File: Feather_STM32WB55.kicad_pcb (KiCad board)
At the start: 4 copper layers, 52.5 x 22.9 mm, 50 parts, among them J1 JST-SH Qwiic, J2 Conn_Battery, J4 Conn_Right, J5 USB_C_Receptacle_USB2.0, J6 Conn_Left, Q1 NTR4171PT1G, SW1 SMD-BUTTON-TOP-DHT-4235A_4P-4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, U1 MCP73831-2-OT, U2 AP2112K-3.3, U3 STM32WB55CGU6, U4 USBLC6-2SC6, Y1 32Mhz

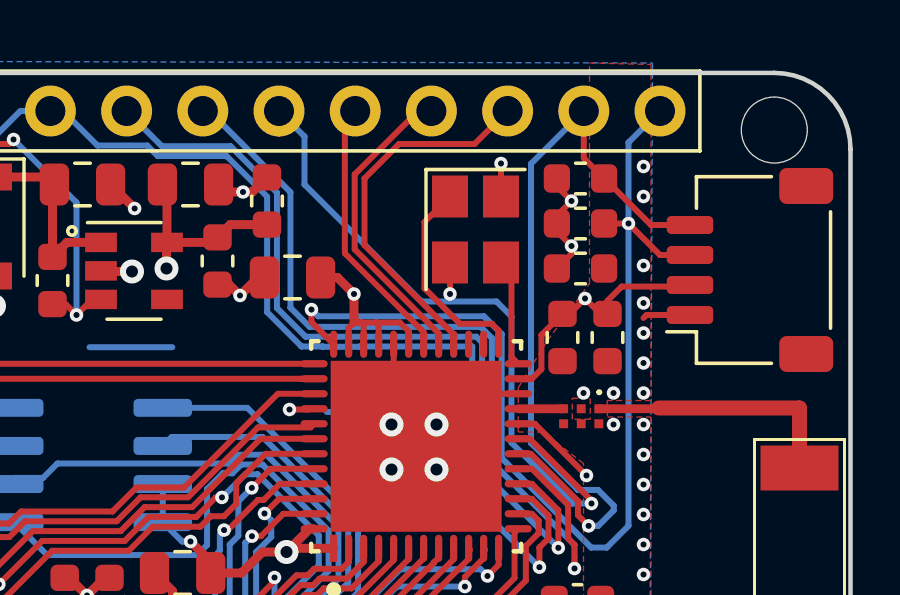
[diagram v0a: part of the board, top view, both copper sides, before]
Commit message: fix: repair STM32WB55 short and restore project libraries (#1)
* docs: improve project discovery and reuse guidance

Describe the historical design and available artifacts from repository evidence. Keep hardware and fabrication outputs unchanged, preserve third-party rights, and make unresolved setup and validation limits visible.

* docs: record completed discoverability delivery

* fix: clear the D10 ground short and restore legacy libraries

Move the overlapping ground via using a controlled before/after zone-refilled DRC comparison. Recover original dependencies and align component identifiers without redesigning the land pattern or guessing the physical stackup. Keep historical fabrication outputs explicitly separate from corrected source.

* docs: record completed source audit delivery

* docs: qualify nightly netlist validation by library resolution

Independent export checks show nightly legacy global-library resolution omits the USB shield pin despite identical cached and global pin geometry. Document the exact cache-only invocation and retain the source without speculative wiring changes.
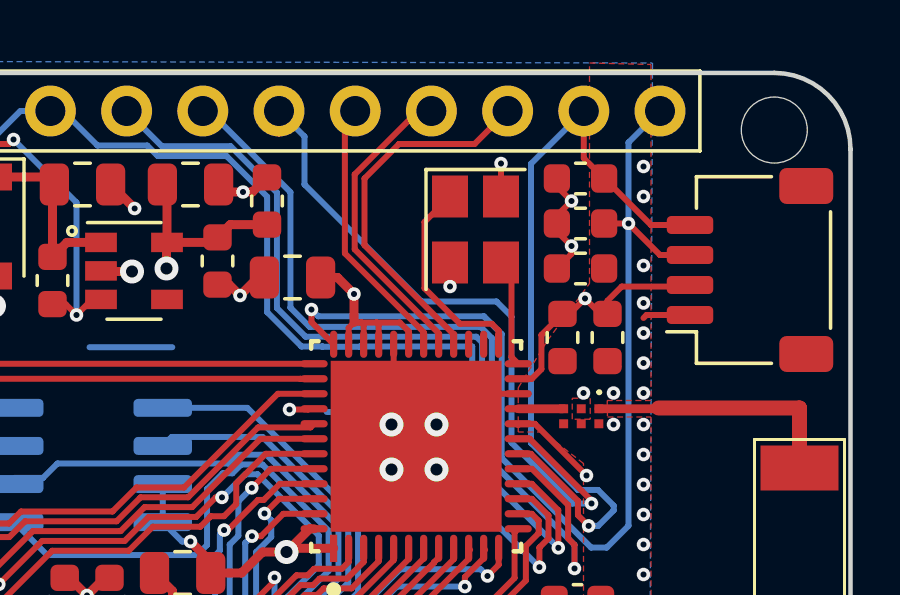
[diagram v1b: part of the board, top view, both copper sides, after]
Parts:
- ANT1: footprint FR05S1N0102 -> Makeristic-KiCad-Library:FR05S1N0102
- FL1: footprint MLPFWB5501E3 -> Makeristic-KiCad-Library:MLPFWB5501E3
- renumbered SWD to J3, FLASH to U5
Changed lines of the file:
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@@
     )
   )
-  (module FR05S1N0102 (layer F.Cu)
+  (module Makeristic-KiCad-Library:FR05S1N0102 (layer F.Cu)
     (at 176.1 97 270)
     (descr FR05-S1-N-0-102-1)
@@
     (pad 2 smd rect (at 2.55 0 270) (size 1.5 2.6) (layers F.Cu F.Paste F.Mask)
       (net 58 "Net-(ANT1-Pad2)"))
-    (model FR05-S1-N-0-102.stp
+    (model ${KIPRJMOD}/../Makeristic-KiCad-Library/Makeristic-KiCad-Library.3dshapes/FR05-S1-N-0-102.stp
       (at (xyz 0 0 0))
       (scale (xyz 1 1 1))
@@
     )
   )
-  (module MLPFWB5501E3 (layer F.Cu)
+  (module Makeristic-KiCad-Library:MLPFWB5501E3 (layer F.Cu)
     (at 168.825 92.725 270)
     (descr MLPF-WB55-01E3-2)
@@
     (pad 6 smd rect (at 0.25 -0.587) (size 0.3 0.3) (layers F.Cu F.Paste F.Mask)
       (net 56 GND))
-    (model MLPF-WB55-01E3.stp
+    (model ${KIPRJMOD}/../Makeristic-KiCad-Library/Makeristic-KiCad-Library.3dshapes/MLPF-WB55-01E3.stp
       (at (xyz 0 0 0))
       (scale (xyz 1 1 1))
@@
     (pad 1 smd rect (at -3.401247 -2.75 90) (size 0.909637 0.242474) (layers F.Cu F.Paste F.Mask)
       (net 57 VDD))
-    (model eec.models/STMicroelectronics_-_STM32WB55CGU6.step
+    (model ${KIPRJMOD}/../Makeristic-KiCad-Library/Makeristic-KiCad-Library.3dshapes/STMicroelectronics_-_STM32WB55CGU6.step
       (at (xyz 0 0 0))
       (scale (xyz 1 1 1))
@@
     (tags "Surface mounted pin header SMD 2x05 1.00mm double row")
     (attr smd)
-    (fp_text reference SWD (at 0 3.56) (layer B.SilkS)
+    (fp_text reference J3 (at 0 3.56) (layer B.SilkS)
       (effects (font (size 1 1) (thickness 0.15)) (justify mirror))
     )
@@
     (tags "SOIC SO")
     (attr smd)
-    (fp_text reference FLASH (at 0 3.4) (layer B.SilkS)
+    (fp_text reference U5 (at 0 3.4) (layer B.SilkS)
       (effects (font (size 1 1) (thickness 0.15)) (justify mirror))
     )
@@
   (segment (start 170.6 100.3) (end 170.9 100) (width 0.2) (layer F.Cu) (net 56))
   (segment (start 169.4875 100.3) (end 170.6 100.3) (width 0.2) (layer F.Cu) (net 56))
-  (via (at 164.45 88.65) (size 0.45) (drill 0.2) (layers F.Cu B.Cu) (net 56))
-  (segment (start 164.45 87.6) (end 164.45 88.44799) (width 0.2) (layer F.Cu) (net 56))
+  (via (at 164.45 88.4) (size 0.45) (drill 0.2) (layers F.Cu B.Cu) (net 56))
+  (segment (start 164.45 87.6) (end 164.45 88.4) (width 0.2) (layer F.Cu) (net 56))
   (via (at 153.85 87.9) (size 0.8) (drill 0.4) (layers F.Cu B.Cu) (net 56))
   (segment (start 152.836 87.9) (end 152.816 87.88) (width 0.3) (layer F.Cu) (net 56))
